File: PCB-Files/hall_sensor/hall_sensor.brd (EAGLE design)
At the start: 6.3 x 4 mm, 5 parts

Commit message: init board layout
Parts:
- moved HALL 0.20 mm to (3.23, 1.64)
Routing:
- net VCC: track 1.63 -> 5.08 mm
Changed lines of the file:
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@@
 <setting verticaltext="up"/>
 </settings>
-<grid distance="0.1" unitdist="mm" unit="mm" style="lines" multiple="1" display="yes" altdistance="0.025" altunitdist="inch" altunit="inch"/>
+<grid distance="0.01" unitdist="mm" unit="mm" style="lines" multiple="1" display="yes" altdistance="0.025" altunitdist="inch" altunit="inch"/>
 <layers>
 <layer number="1" name="Top" color="4" fill="1" visible="yes" active="yes"/>
@@
 <layer number="46" name="Milling" color="3" fill="1" visible="yes" active="yes"/>
 <layer number="47" name="Measures" color="7" fill="1" visible="yes" active="yes"/>
-<layer number="48" name="Document" color="7" fill="1" visible="yes" active="yes"/>
+<layer number="48" name="Document" color="14" fill="1" visible="yes" active="yes"/>
 <layer number="49" name="Reference" color="7" fill="1" visible="yes" active="yes"/>
 <layer number="50" name="dxf" color="7" fill="1" visible="no" active="no"/>
@@
 <layer number="57" name="tCAD" color="7" fill="1" visible="no" active="no"/>
 <layer number="58" name="bCAD" color="7" fill="1" visible="no" active="no"/>
+<layer number="59" name="tCarbon" color="7" fill="1" visible="no" active="no"/>
+<layer number="60" name="bCarbon" color="7" fill="1" visible="no" active="no"/>
 <layer number="90" name="Modules" color="5" fill="1" visible="no" active="no"/>
 <layer number="91" name="Nets" color="2" fill="1" visible="no" active="no"/>
@@
 <layer number="115" name="16" color="14" fill="1" visible="yes" active="yes"/>
 <layer number="116" name="Patch_BOT" color="9" fill="4" visible="yes" active="yes"/>
+<layer number="118" name="Rect_Pads" color="7" fill="1" visible="no" active="no"/>
 <layer number="121" name="_tsilk" color="7" fill="1" visible="yes" active="yes"/>
 <layer number="122" name="_bsilk" color="7" fill="1" visible="yes" active="yes"/>
@@
 <layer number="127" name="_tValues" color="7" fill="1" visible="yes" active="yes"/>
 <layer number="128" name="_bValues" color="7" fill="1" visible="yes" active="yes"/>
+<layer number="129" name="Mask" color="7" fill="1" visible="yes" active="yes"/>
 <layer number="131" name="tAdjust" color="7" fill="1" visible="yes" active="yes"/>
 <layer number="132" name="bAdjust" color="7" fill="1" visible="yes" active="yes"/>
@@
 <layer number="223" name="223bmp" color="24" fill="1" visible="no" active="no"/>
 <layer number="224" name="224bmp" color="25" fill="1" visible="no" active="no"/>
+<layer number="225" name="225bmp" color="7" fill="1" visible="yes" active="yes"/>
+<layer number="226" name="226bmp" color="7" fill="1" visible="yes" active="yes"/>
+<layer number="227" name="227bmp" color="7" fill="1" visible="yes" active="yes"/>
+<layer number="228" name="228bmp" color="7" fill="1" visible="yes" active="yes"/>
+<layer number="229" name="229bmp" color="7" fill="1" visible="yes" active="yes"/>
+<layer number="230" name="230bmp" color="7" fill="1" visible="yes" active="yes"/>
+<layer number="231" name="Eagle3D_PG1" color="7" fill="1" visible="no" active="no"/>
+<layer number="232" name="Eagle3D_PG2" color="7" fill="1" visible="no" active="no"/>
+<layer number="233" name="Eagle3D_PG3" color="7" fill="1" visible="no" active="no"/>
 <layer number="248" name="Housing" color="7" fill="1" visible="yes" active="yes"/>
 <layer number="249" name="Edge" color="7" fill="1" visible="yes" active="yes"/>
@@
 <layer number="251" name="SMDround" color="12" fill="11" visible="no" active="no"/>
 <layer number="254" name="cooling" color="7" fill="1" visible="yes" active="yes"/>
+<layer number="255" name="routoute" color="7" fill="1" visible="yes" active="yes"/>
 </layers>
 <board>
@@
 <wire x1="0" y1="3.95" x2="1.1" y2="3.95" width="0.0254" layer="20"/>
 <wire x1="5.25" y1="3.95" x2="1.1" y2="3.95" width="0.0254" layer="20" curve="-81.9"/>
+<circle x="3.18" y="6.61" radius="3.302" width="0" layer="48"/>
 </plain>
 <attributes>
@@
 </autorouter>
 <elements>
-<element name="HALL" library="Andy_Sigler" package="SOT23-3" value="HALLEFFECT-A1326" x="3.025" y="1.6375" smashed="yes" rot="R90">
-<attribute name="NAME" x="1.247" y="0.812" size="0.4064" layer="25" rot="R90"/>
-<attribute name="VALUE" x="3.2155" y="0.6215" size="0.4064" layer="27" rot="R90"/>
+<element name="HALL" library="Andy_Sigler" package="SOT23-3" value="HALLEFFECT-A1326" x="3.225" y="1.6375" smashed="yes" rot="R90">
+<attribute name="NAME" x="1.447" y="0.812" size="0.4064" layer="25" rot="R90"/>
 </element>
 <element name="TP1" library="testpad" package="TP10SQ" value="TPTP10SQ" x="5.65" y="1.95" smashed="yes">
 <attribute name="TP_SIGNAL_NAME" value="" x="5.65" y="0.045" size="1" layer="37"/>
-<attribute name="NAME" x="5.1499" y="2.4999" size="1.27" layer="25"/>
 <attribute name="VALUE" x="5.142" y="1.315" size="0.0254" layer="27"/>
 </element>
 <element name="TP2" library="testpad" package="TP10SQ" value="TPTP10SQ" x="5.65" y="3.2" smashed="yes">
 <attribute name="TP_SIGNAL_NAME" value="" x="5.65" y="1.295" size="1" layer="37"/>
-<attribute name="NAME" x="5.1499" y="3.7499" size="1.27" layer="25"/>
 <attribute name="VALUE" x="5.142" y="2.565" size="0.0254" layer="27"/>
 </element>
 <element name="TP3" library="testpad" package="TP10SQ" value="TPTP10SQ" x="5.65" y="0.7" smashed="yes">
 <attribute name="TP_SIGNAL_NAME" value="" x="5.65" y="-1.205" size="1" layer="37"/>
-<attribute name="NAME" x="5.1499" y="1.2499" size="1.27" layer="25"/>
 <attribute name="VALUE" x="5.142" y="0.065" size="0.0254" layer="27"/>
 </element>
-<element name="C1" library="SparkFun" package="0603-CAP" value="0.1uF" x="0.8" y="1.7" smashed="yes" rot="R270">
-<attribute name="NAME" x="1.562" y="2.589" size="0.4064" layer="25" font="vector" rot="R270"/>
-<attribute name="VALUE" x="-0.343" y="2.716" size="0.4064" layer="27" font="vector" rot="R270"/>
-</element>
+<element name="C1" library="SparkFun" package="0603-CAP" value="0.1uF" x="0.8" y="1.7" smashed="yes" rot="R270"/>
 </elements>
 <signals>
@@
 <contactref element="HALL" pad="1"/>
 <contactref element="TP3" pad="TP"/>
-<wire x1="4.025" y1="0.6875" x2="5.6375" y2="0.6875" width="0.8128" layer="1"/>
-<wire x1="5.6375" y1="0.6875" x2="5.65" y2="0.7" width="0.8128" layer="1"/>
+<wire x1="4.225" y1="0.6875" x2="5.6375" y2="0.6875" width="0.6096" layer="1"/>
+<wire x1="5.6375" y1="0.6875" x2="5.65" y2="0.7" width="0.6096" layer="1"/>
 <contactref element="C1" pad="2"/>
-<wire x1="0.8" y1="0.85" x2="5.65" y2="0.7" width="0" layer="19" extent="1-1"/>
+<wire x1="4.225" y1="0.6875" x2="3.6875" y2="0.6875" width="0.6096" layer="1"/>
+<wire x1="3.6875" y1="0.6875" x2="3.5" y2="0.5" width="0.6096" layer="1"/>
+<wire x1="3.5" y1="0.5" x2="1.15" y2="0.5" width="0.6096" layer="1"/>
+<wire x1="1.15" y1="0.5" x2="0.8" y2="0.85" width="0.6096" layer="1"/>
 </signal>
 <signal name="GND">
 <contactref element="HALL" pad="3"/>
 <contactref element="TP1" pad="TP"/>
-<wire x1="5.65" y1="1.95" x2="5.025" y2="1.95" width="0.8128" layer="1"/>
-<wire x1="5.025" y1="1.95" x2="4.7" y2="1.6375" width="0.8128" layer="1"/>
-<wire x1="4.7" y1="1.6375" x2="1.925" y2="1.6375" width="0.8128" layer="1"/>
-<polygon width="0.3048" layer="1">
+<wire x1="5.65" y1="1.95" x2="5.125" y2="1.95" width="0.6096" layer="1"/>
+<wire x1="5.125" y1="1.95" x2="4.7" y2="1.6375" width="0.6096" layer="1"/>
+<wire x1="4.7" y1="1.6375" x2="2.125" y2="1.6375" width="0.6096" layer="1"/>
+<polygon width="0.3048" layer="1" thermals="no">
 <vertex x="-1" y="8"/>
 <vertex x="7" y="8"/>
@@
 </polygon>
 <contactref element="C1" pad="1"/>
-<wire x1="5.65" y1="1.95" x2="0.8" y2="2.55" width="0" layer="19" extent="1-1"/>
 </signal>
 <signal name="N$2">
@@
 <contactref element="HALL" pad="2"/>
 <contactref element="TP2" pad="TP"/>
-<wire x1="4.025" y1="2.5875" x2="4.3" y2="2.5875" width="0.8128" layer="1"/>
-<wire x1="4.3" y1="2.5875" x2="4.8875" y2="2.9875" width="0.8128" layer="1"/>
-<wire x1="4.8875" y1="2.9875" x2="5.55" y2="3.1" width="0.8128" layer="1"/>
-<wire x1="5.55" y1="3.1" x2="5.65" y2="3.2" width="0.8128" layer="1"/>
+<wire x1="4.225" y1="2.5875" x2="4.3" y2="2.5875" width="0.6096" layer="1"/>
+<wire x1="4.3" y1="2.5875" x2="4.8875" y2="2.9875" width="0.6096" layer="1"/>
+<wire x1="4.8875" y1="2.9875" x2="5.55" y2="3.1" width="0.6096" layer="1"/>
+<wire x1="5.55" y1="3.1" x2="5.65" y2="3.2" width="0.6096" layer="1"/>
 </signal>
 </signals>

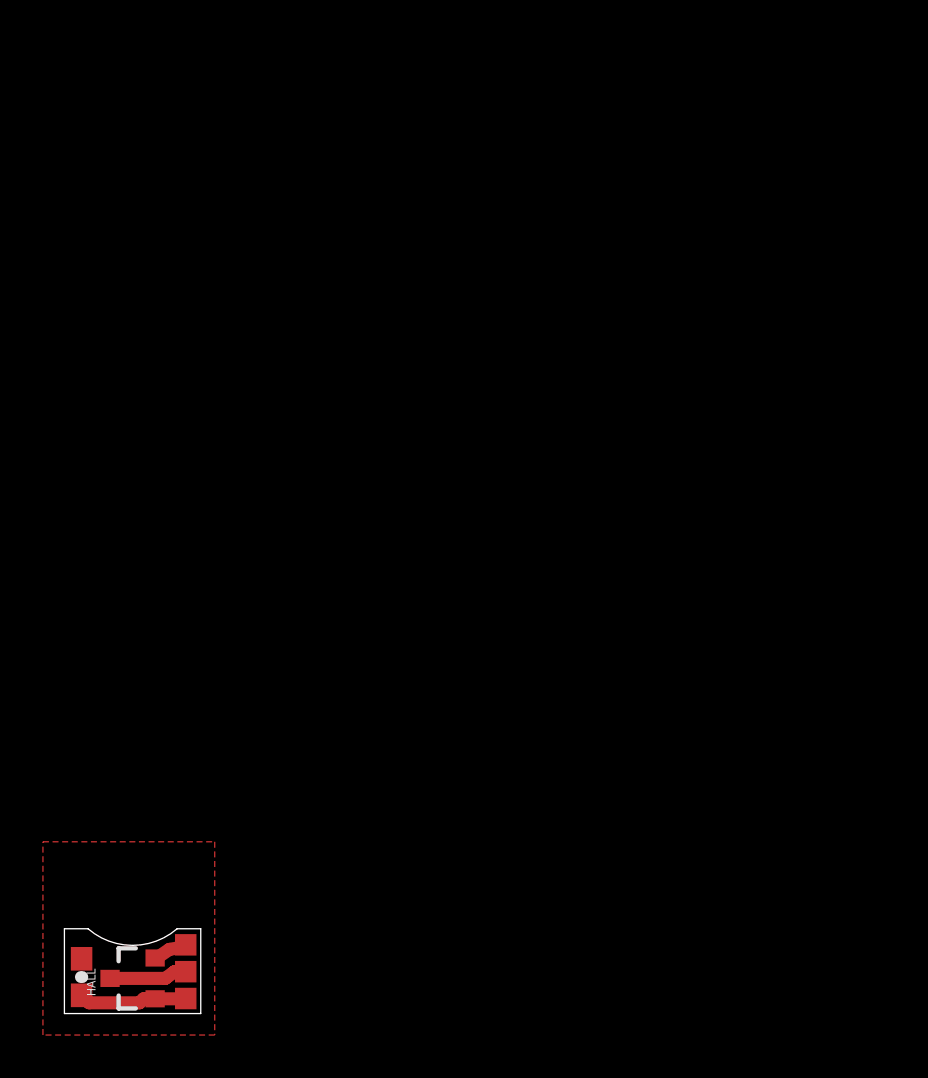
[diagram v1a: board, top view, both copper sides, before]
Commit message: esp32 touch sketch tests
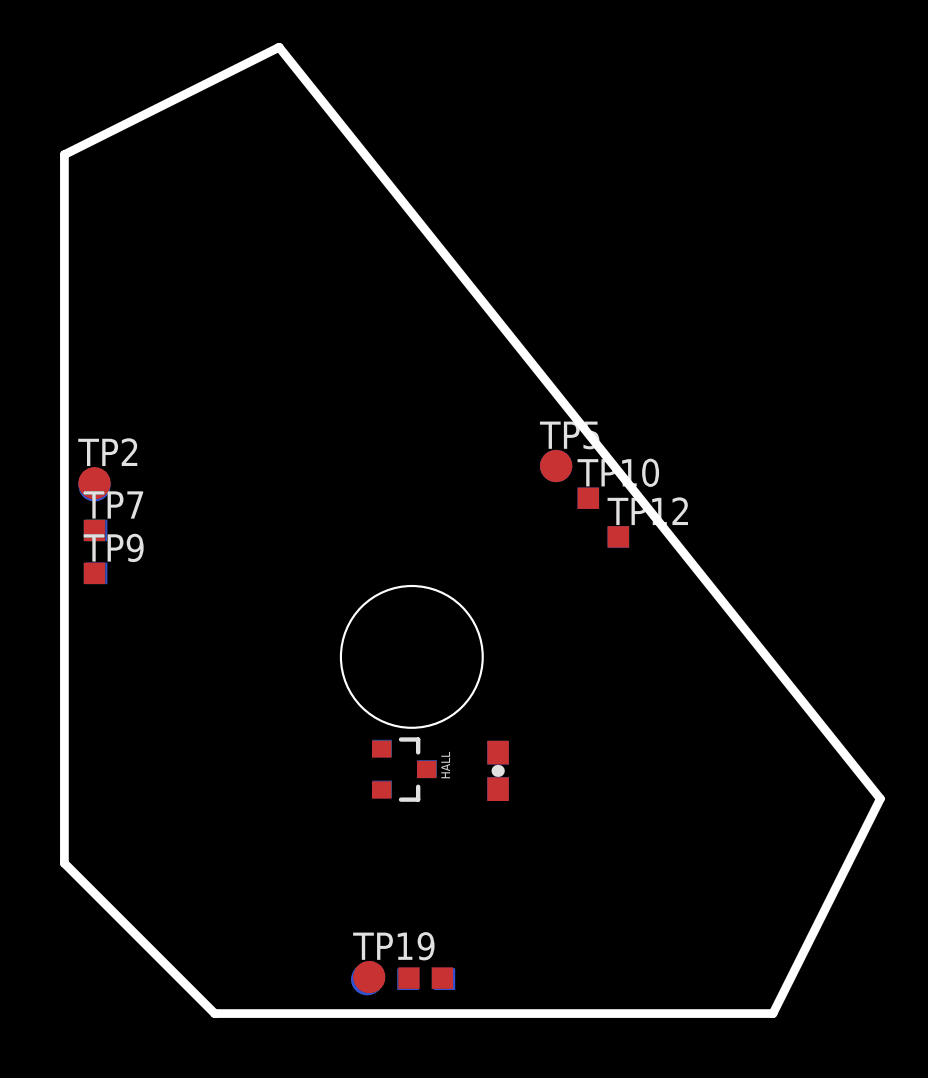
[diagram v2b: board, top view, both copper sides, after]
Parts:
- added C2: 0.1uF, SparkFun:0603-CAP
- added HALL1: HALLEFFECT-A1326, Andy_Sigler:SOT23-3
- added TP10, TP12, TP13, TP15, TP16, TP18, TP4, TP6, TP7, TP9: TPTP10SQ, testpad:TP10SQ
- added TP11, TP14, TP19, TP5, TP8: TPTP15R, testpad:TP15R
- TP2: value TPTP10SQ -> TPTP15R; device testpad:TP10SQ -> testpad:TP15R
- moved TP2 21.9 mm to (1.40, 24.7)
- moved C1 21.6 mm to (20.2, 11.3), turned to 90 degrees
- moved HALL 15.9 mm to (15.8, 11.4), turned to 270 degrees
- moved TP3 12.0 mm to (17.6, 1.65), turned to 90 degrees
- moved TP1 10.4 mm to (16.1, 1.65), turned to 90 degrees
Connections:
- removed net GND: C1.1, HALL.3, TP1.TP
- removed net VCC: C1.2, HALL.1, TP3.TP
- new net GND1: C1.1, HALL.3, TP1.TP, TP10.TP, TP7.TP
- new net GND2: C2.1, HALL1.3, TP13.TP, TP16.TP, TP4.TP
- new net SIG2: HALL1.2, TP11.TP, TP14.TP, TP8.TP
- new net VCC1: C1.2, HALL.1, TP12.TP, TP3.TP, TP9.TP
- new net VCC2: C2.2, HALL1.1, TP15.TP, TP18.TP, TP6.TP
- net SIG1: now also TP19.TP, TP5.TP
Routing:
- net VCC: track 5.08 -> 0.00 mm
- net GND: track 3.63 -> 0.00 mm
- net SIG1: track 1.60 -> 0.00 mm
- removed copper zone on layer 1, net GND
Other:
- board size 6.3 x 4 mm -> 38 x 45 mm
